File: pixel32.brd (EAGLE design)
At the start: 67 parts, among them CON1 DS1066-07M-SIDE, CON2 DS1066-07M-SIDE, IC1 STM32F030K6TX-LQFP32(7X7), IC2 TPS54260, IC3 ST3485SOIC8, IC4 ESDA6V1L, IC5 3.3, IC6 MC74VHC1GT125, IC7 MC74VHC1GT125, Q1 FDC6420C

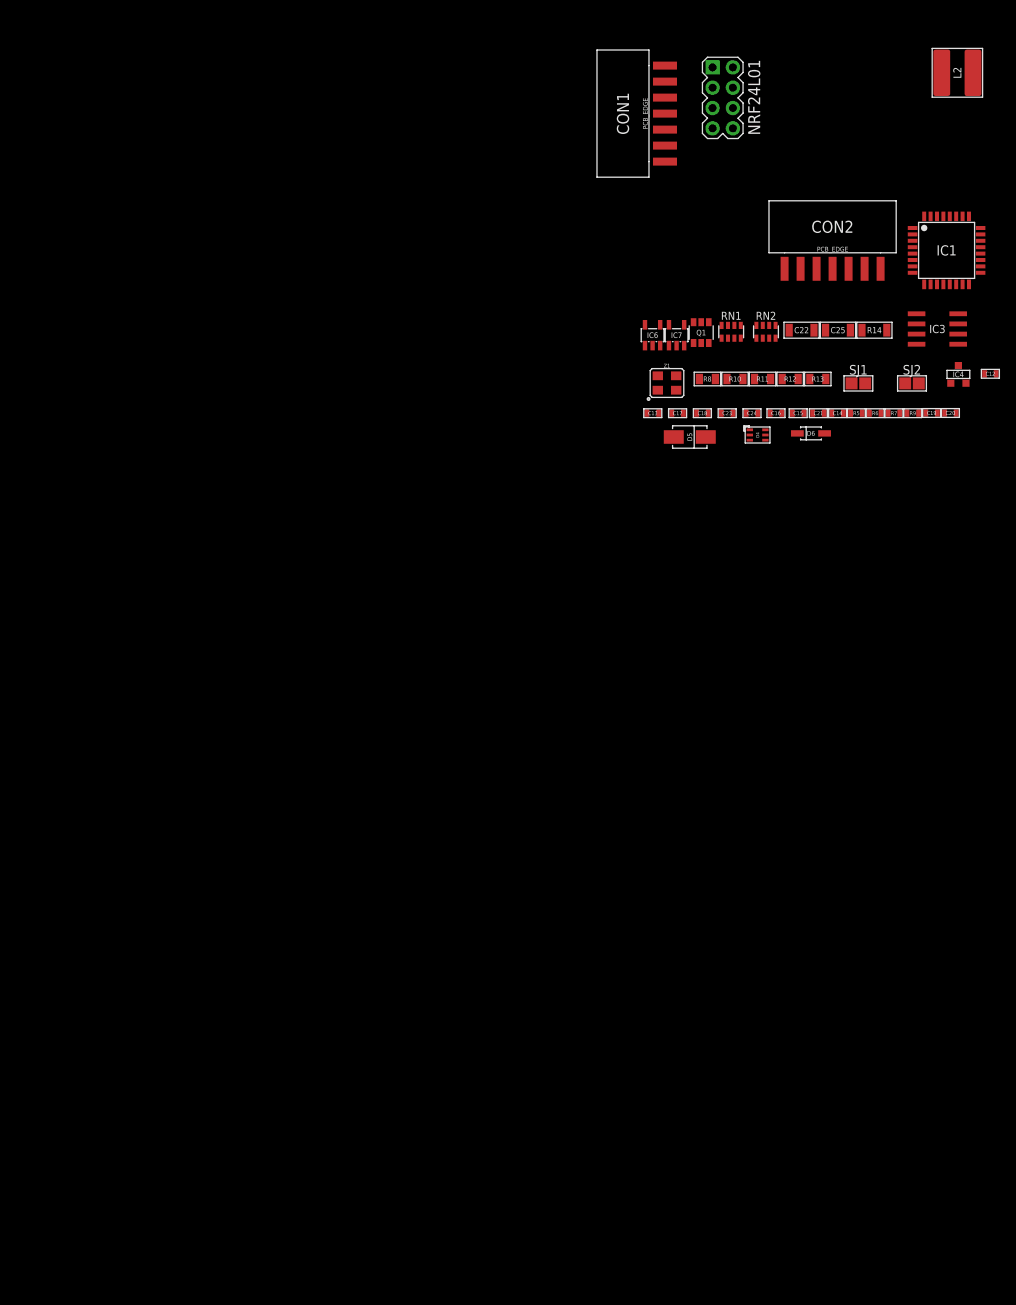
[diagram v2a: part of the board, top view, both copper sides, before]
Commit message: Led driver schematics added
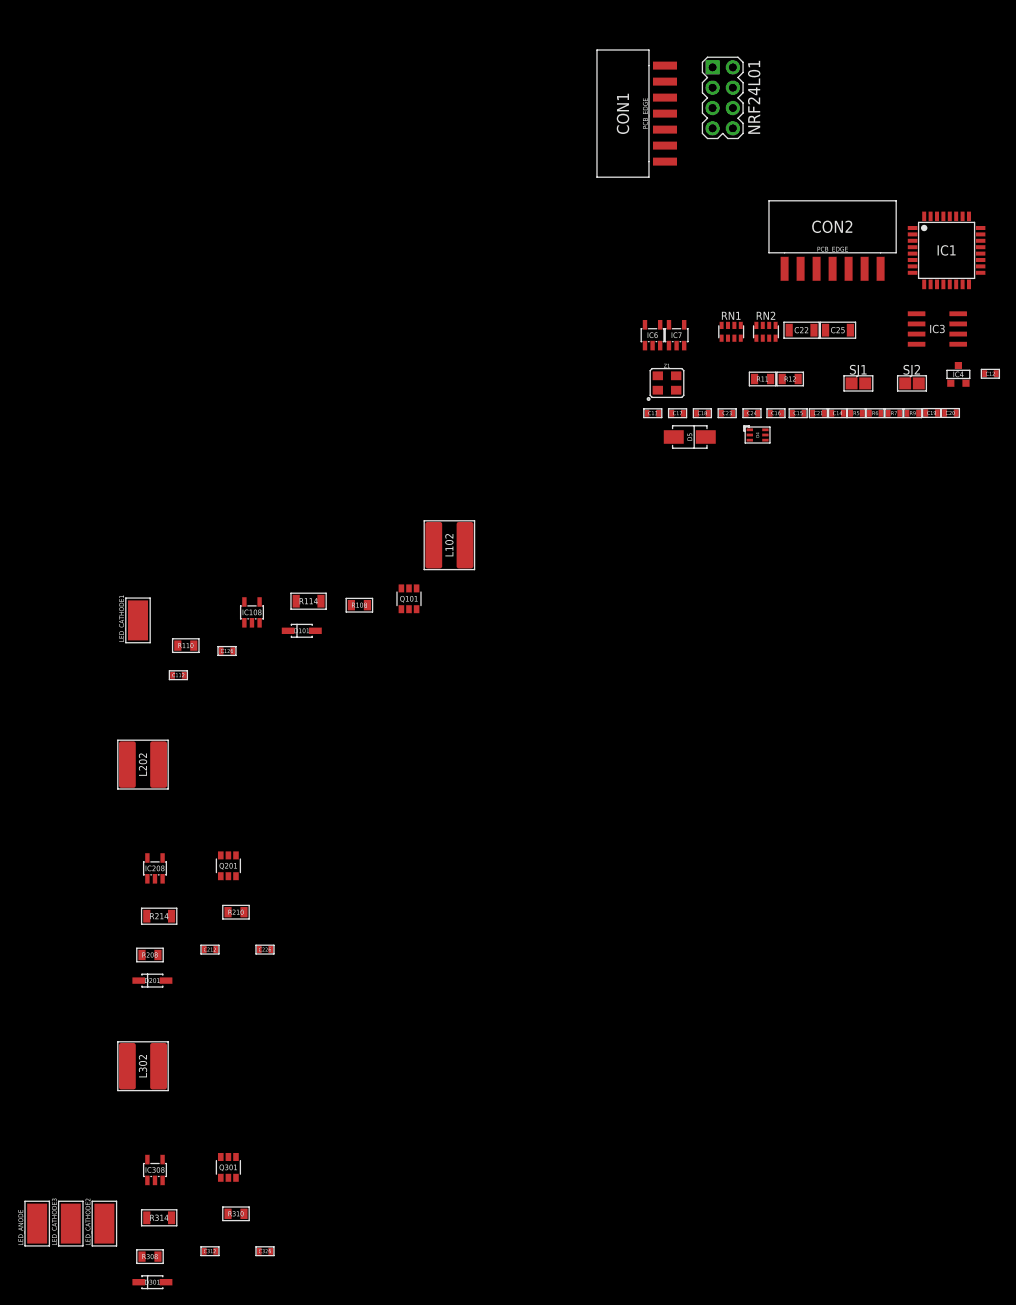
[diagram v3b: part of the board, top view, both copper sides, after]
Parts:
- removed D6: CRS08-SOD123, eth_conv_master_lib:SOD123
- removed L2: 47UH, power_inductors:SDR0604
- removed Q1: FDC6420C, pixel_masterlib:SOT23-6
- removed R10, R8: 22R, rc:R0805
- removed R13: 10K, rc:R0805
- removed R14: 2R, rc:R1206
- added C112, C212, C312: 100 nF, rc:C0603
- added C126, C226, C326: 1 uF, rc:C0603
- added D101, D201, D301: CRS08-SOD123, FMU_masterlib:SOD123
- added IC108, IC208, IC308: IRS44273L, pixel_masterlib:SOT23-5
- added L102, L202, L302: 47UH, power_inductors:SDR0604
- added LED_ANODE, LED_CATHODE1, LED_CATHODE2, LED_CATHODE3: WIREPADSMD5-2,5, valenok_master_library:5-2,5
- added Q101, Q201, Q301: FDC6420C, pixel_masterlib:SOT23-6
- added R108, R110, R208, R210, R308, R310: 22R, rc:R0805
- added R114, R214, R314: 2R, rc:R1206
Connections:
- new net LED_DRIVER1:N$1: Q101.1, R108.2
- new net LED_DRIVER1:N$2: D101.A, L102.1, Q101.6
- new net LED_DRIVER1:N$3: IC108.3, IC108.4, R108.1, R110.2
- new net LED_DRIVER2:N$1: Q201.1, R208.2
- new net LED_DRIVER2:N$2: D201.A, L202.1, Q201.6
- new net LED_DRIVER2:N$3: IC208.3, IC208.4, R208.1, R210.2
- new net LED_DRIVER3:N$1: Q301.1, R308.2
- new net LED_DRIVER3:N$2: D301.A, L302.1, Q301.6
- new net LED_DRIVER3:N$3: IC308.3, IC308.4, R308.1, R310.2
- new net N$10: D101.C, LED_CATHODE1.1
- new net N$25: C312.2, Q301.5, R314.P$2
- new net N$26: C126.2, C226.2, C326.2, IC108.5, IC208.5, IC308.5
- new net N$27: C212.2, Q201.5, R214.P$2
- new net N$28: C112.1, C126.1, C212.1, C226.1, C312.1, C326.1, IC108.2, IC208.2, IC308.2, R114.P$1, R214.P$1, R314.P$1
- new net N$29: IC208.1, R210.1
- new net N$30: C112.2, Q101.5, R114.P$2
- new net N$31: IC108.1, R110.1
- net GND: no longer D6.A, Q1.5, R14.P$1
- net LED1_PWM: no longer R8.1
- net N$20: now also L102.2, L202.2, L302.2, LED_ANODE.1; no longer Q1.1, R8.2
- net N$21: now also D201.C, LED_CATHODE2.1; no longer Q1.3, R10.2, R13.2
- net N$23: now also D301.C, LED_CATHODE3.1; no longer Q1.6, R10.1
- net N$24: now also IC308.1, R310.1; no longer D6.C, L2.1, Q1.2
- net VDD_12V: no longer Q1.4, R13.1

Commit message: blah
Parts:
- added TP101, TP102, TP103, TP201, TP202, TP203, TP301, TP302, TP303: PAD.05, pixhawk2:PAD.05X.05
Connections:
- net LED_DRIVER1:N$2: now also TP102.P$1
- net LED_DRIVER2:N$2: now also TP202.P$1
- net LED_DRIVER3:N$2: now also TP302.P$1
- net N$10: now also L102.2; no longer D101.C
- net N$20: now also D101.C, D201.C, D301.C; no longer L102.2, L202.2, L302.2
- net N$21: now also L202.2; no longer D201.C
- net N$23: now also L302.2; no longer D301.C
- net N$24: now also TP301.P$1
- net N$25: now also TP303.P$1
- net N$27: now also TP203.P$1
- net N$29: now also TP201.P$1
- net N$30: now also TP103.P$1
- net N$31: now also TP101.P$1
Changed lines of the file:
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@@
 <element name="LED_CATHODE3" library="valenok_master_library" package="5-2,5" value="WIREPADSMD5-2,5" x="-79.2" y="-170.375"/>
 <element name="LED_ANODE" library="valenok_master_library" package="5-2,5" value="WIREPADSMD5-2,5" x="-83.4" y="-170.375"/>
+<element name="TP101" library="pixhawk2" package="PAD.05X.05" value="PAD.05" x="-83.85" y="-179.75">
+<attribute name="BOM" value="EXCLUDE" x="-83.85" y="-179.625" size="1.778" layer="27" display="off"/>
+<attribute name="PARTNO" value="*" x="-83.85" y="-179.625" size="1.778" layer="27" display="off"/>
+</element>
+<element name="TP201" library="pixhawk2" package="PAD.05X.05" value="PAD.05" x="-83.85" y="-181.8">
+<attribute name="BOM" value="EXCLUDE" x="-83.85" y="-181.55" size="1.778" layer="27" display="off"/>
+<attribute name="PARTNO" value="*" x="-83.85" y="-181.55" size="1.778" layer="27" display="off"/>
+</element>
+<element name="TP301" library="pixhawk2" package="PAD.05X.05" value="PAD.05" x="-83.85" y="-183.85">
+<attribute name="BOM" value="EXCLUDE" x="-83.85" y="-183.475" size="1.778" layer="27" display="off"/>
+<attribute name="PARTNO" value="*" x="-83.85" y="-183.475" size="1.778" layer="27" display="off"/>
+</element>
+<element name="TP102" library="pixhawk2" package="PAD.05X.05" value="PAD.05" x="-83.85" y="-185.775">
+<attribute name="BOM" value="EXCLUDE" x="-83.85" y="-185.775" size="1.778" layer="27" display="off"/>
+<attribute name="PARTNO" value="*" x="-83.85" y="-185.775" size="1.778" layer="27" display="off"/>
+</element>
+<element name="TP202" library="pixhawk2" package="PAD.05X.05" value="PAD.05" x="-83.85" y="-187.7">
+<attribute name="BOM" value="EXCLUDE" x="-83.85" y="-187.7" size="1.778" layer="27" display="off"/>
+<attribute name="PARTNO" value="*" x="-83.85" y="-187.7" size="1.778" layer="27" display="off"/>
+</element>
+<element name="TP302" library="pixhawk2" package="PAD.05X.05" value="PAD.05" x="-83.85" y="-189.625">
+<attribute name="BOM" value="EXCLUDE" x="-83.85" y="-189.625" size="1.778" layer="27" display="off"/>
+<attribute name="PARTNO" value="*" x="-83.85" y="-189.625" size="1.778" layer="27" display="off"/>
+</element>
+<element name="TP103" library="pixhawk2" package="PAD.05X.05" value="PAD.05" x="-83.85" y="-191.55">
+<attribute name="BOM" value="EXCLUDE" x="-83.85" y="-191.55" size="1.778" layer="27" display="off"/>
+<attribute name="PARTNO" value="*" x="-83.85" y="-191.55" size="1.778" layer="27" display="off"/>
+</element>
+<element name="TP203" library="pixhawk2" package="PAD.05X.05" value="PAD.05" x="-83.85" y="-193.475">
+<attribute name="BOM" value="EXCLUDE" x="-83.85" y="-193.475" size="1.778" layer="27" display="off"/>
+<attribute name="PARTNO" value="*" x="-83.85" y="-193.475" size="1.778" layer="27" display="off"/>
+</element>
+<element name="TP303" library="pixhawk2" package="PAD.05X.05" value="PAD.05" x="-83.85" y="-195.4">
+<attribute name="BOM" value="EXCLUDE" x="-83.85" y="-195.4" size="1.778" layer="27" display="off"/>
+<attribute name="PARTNO" value="*" x="-83.85" y="-195.4" size="1.778" layer="27" display="off"/>
+</element>
 </elements>
 <signals>
@@
 <contactref element="D101" pad="A"/>
 <contactref element="L102" pad="1"/>
+<contactref element="TP102" pad="P$1"/>
 <wire x1="-37.875" y1="-90.975" x2="-48.625" y2="-96.275" width="0" layer="19" extent="1-1"/>
 <wire x1="-33.825" y1="-85.575" x2="-37.875" y2="-90.975" width="0" layer="19" extent="1-1"/>
+<wire x1="-83.85" y1="-185.775" x2="-48.625" y2="-96.275" width="0" layer="19" extent="1-1"/>
 </signal>
 <signal name="LED_DRIVER2:N$1">
@@
 <contactref element="D201" pad="A"/>
 <contactref element="L202" pad="1"/>
+<contactref element="TP202" pad="P$1"/>
 <wire x1="-60.45" y1="-124.35" x2="-67.3" y2="-140" width="0" layer="19" extent="1-1"/>
 <wire x1="-72.125" y1="-113" x2="-60.45" y2="-124.35" width="0" layer="19" extent="1-1"/>
+<wire x1="-83.85" y1="-187.7" x2="-67.3" y2="-140" width="0" layer="19" extent="1-1"/>
 </signal>
 <signal name="LED_DRIVER2:N$3">
@@
 <contactref element="D301" pad="A"/>
 <contactref element="L302" pad="1"/>
+<contactref element="TP302" pad="P$1"/>
 <wire x1="-60.45" y1="-162.05" x2="-67.3" y2="-177.7" width="0" layer="19" extent="1-1"/>
 <wire x1="-72.125" y1="-150.7" x2="-60.45" y2="-162.05" width="0" layer="19" extent="1-1"/>
+<wire x1="-83.85" y1="-189.625" x2="-67.3" y2="-177.7" width="0" layer="19" extent="1-1"/>
 </signal>
 <signal name="LED_DRIVER3:N$3">
@@
 </signal>
 <signal name="N$10">
+<contactref element="LED_CATHODE1" pad="1"/>
+<contactref element="L102" pad="2"/>
+<wire x1="-29.925" y1="-85.575" x2="-70.8" y2="-94.975" width="0" layer="19" extent="1-1"/>
+</signal>
+<signal name="N$20">
+<contactref element="LED_ANODE" pad="1"/>
 <contactref element="D101" pad="C"/>
-<contactref element="LED_CATHODE1" pad="1"/>
-<wire x1="-52.025" y1="-96.275" x2="-70.8" y2="-94.975" width="0" layer="19" extent="1-1"/>
-</signal>
-<signal name="N$20">
-<contactref element="L102" pad="2"/>
-<contactref element="L302" pad="2"/>
-<contactref element="L202" pad="2"/>
-<contactref element="LED_ANODE" pad="1"/>
-<wire x1="-68.225" y1="-150.7" x2="-83.4" y2="-170.375" width="0" layer="19" extent="1-1"/>
-<wire x1="-68.225" y1="-113" x2="-68.225" y2="-150.7" width="0" layer="19" extent="1-1"/>
-<wire x1="-29.925" y1="-85.575" x2="-68.225" y2="-113" width="0" layer="19" extent="1-1"/>
+<contactref element="D201" pad="C"/>
+<contactref element="D301" pad="C"/>
+<wire x1="-70.7" y1="-177.7" x2="-83.4" y2="-170.375" width="0" layer="19" extent="1-1"/>
+<wire x1="-70.7" y1="-140" x2="-83.4" y2="-170.375" width="0" layer="19" extent="1-1"/>
+<wire x1="-52.025" y1="-96.275" x2="-70.7" y2="-140" width="0" layer="19" extent="1-1"/>
 </signal>
 <signal name="N$21">
 <contactref element="LED_CATHODE2" pad="1"/>
-<contactref element="D201" pad="C"/>
-<wire x1="-70.7" y1="-140" x2="-75" y2="-170.375" width="0" layer="19" extent="1-1"/>
+<contactref element="L202" pad="2"/>
+<wire x1="-68.225" y1="-113" x2="-75" y2="-170.375" width="0" layer="19" extent="1-1"/>
 </signal>
 <signal name="N$23">
 <contactref element="LED_CATHODE3" pad="1"/>
-<contactref element="D301" pad="C"/>
-<wire x1="-70.7" y1="-177.7" x2="-79.2" y2="-170.375" width="0" layer="19" extent="1-1"/>
+<contactref element="L302" pad="2"/>
+<wire x1="-68.225" y1="-150.7" x2="-79.2" y2="-170.375" width="0" layer="19" extent="1-1"/>
 </signal>
 <signal name="N$24">
 <contactref element="R310" pad="1"/>
 <contactref element="IC308" pad="1"/>
+<contactref element="TP301" pad="P$1"/>
 <wire x1="-59.55" y1="-169.15" x2="-69.625" y2="-164.975" width="0" layer="19" extent="1-1"/>
+<wire x1="-83.85" y1="-183.85" x2="-69.625" y2="-164.975" width="0" layer="19" extent="1-1"/>
 </signal>
 <signal name="N$25">
@@
 <contactref element="Q301" pad="5"/>
 <contactref element="C312" pad="2"/>
+<contactref element="TP303" pad="P$1"/>
 <wire x1="-61.075" y1="-173.825" x2="-66.6" y2="-169.65" width="0" layer="19" extent="1-1"/>
 <wire x1="-59.5" y1="-162.05" x2="-66.6" y2="-169.65" width="0" layer="19" extent="1-1"/>
+<wire x1="-83.85" y1="-195.4" x2="-66.6" y2="-169.65" width="0" layer="19" extent="1-1"/>
 </signal>
 <signal name="N$27">
@@
 <contactref element="Q201" pad="5"/>
 <contactref element="C212" pad="2"/>
+<contactref element="TP203" pad="P$1"/>
 <wire x1="-61.075" y1="-136.125" x2="-66.6" y2="-131.95" width="0" layer="19" extent="1-1"/>
 <wire x1="-59.5" y1="-124.35" x2="-66.6" y2="-131.95" width="0" layer="19" extent="1-1"/>
+<wire x1="-83.85" y1="-193.475" x2="-61.075" y2="-136.125" width="0" layer="19" extent="1-1"/>
 </signal>
 <signal name="N$29">
 <contactref element="R210" pad="1"/>
 <contactref element="IC208" pad="1"/>
+<contactref element="TP201" pad="P$1"/>
 <wire x1="-59.55" y1="-131.45" x2="-69.625" y2="-127.275" width="0" layer="19" extent="1-1"/>
+<wire x1="-83.85" y1="-181.8" x2="-59.55" y2="-131.45" width="0" layer="19" extent="1-1"/>
 </signal>
 <signal name="N$30">
@@
 <contactref element="Q101" pad="5"/>
 <contactref element="C112" pad="2"/>
+<contactref element="TP103" pad="P$1"/>
 <wire x1="-47.925" y1="-92.575" x2="-65.025" y2="-101.825" width="0" layer="19" extent="1-1"/>
 <wire x1="-36.925" y1="-90.975" x2="-47.925" y2="-92.575" width="0" layer="19" extent="1-1"/>
+<wire x1="-83.85" y1="-191.55" x2="-65.025" y2="-101.825" width="0" layer="19" extent="1-1"/>
 </signal>
 <signal name="N$31">
 <contactref element="R110" pad="1"/>
 <contactref element="IC108" pad="1"/>
+<contactref element="TP101" pad="P$1"/>
 <wire x1="-57.5" y1="-95.275" x2="-65.825" y2="-98.125" width="0" layer="19" extent="1-1"/>
+<wire x1="-83.85" y1="-179.75" x2="-65.825" y2="-98.125" width="0" layer="19" extent="1-1"/>
 </signal>
 </signals>
